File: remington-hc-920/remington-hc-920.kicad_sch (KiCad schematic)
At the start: 8 parts, among them M1 Motor_DC, SW1 SW_DPDT_x2

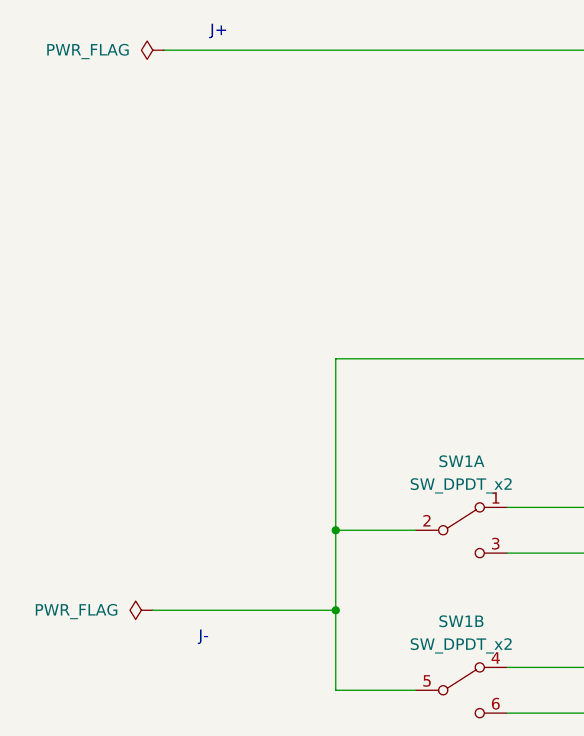
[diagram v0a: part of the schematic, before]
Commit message: Label J+/J- as charging plug input
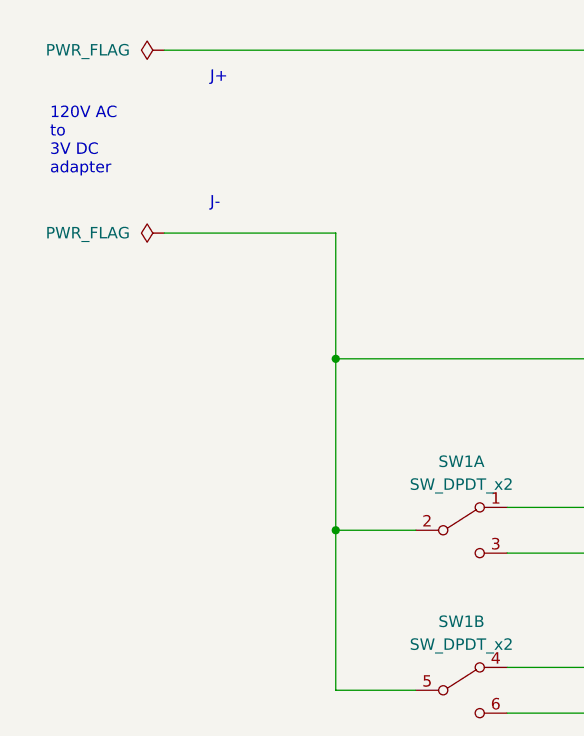
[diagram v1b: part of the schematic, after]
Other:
- note added: "120V AC to 3V DC adapter"
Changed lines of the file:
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@@
   (junction (at 199.39 115.57) (diameter 0) (color 0 0 0 0)
   )
-  (junction (at 99.06 133.35) (diameter 0) (color 0 0 0 0)
-  )
   (junction (at 162.56 121.92) (diameter 0) (color 0 0 0 0)
   )
@@
   (junction (at 99.06 124.46) (diameter 0) (color 0 0 0 0)
   )
+  (junction (at 99.06 105.41) (diameter 0) (color 0 0 0 0)
+  )
   (junction (at 138.43 105.41) (diameter 0) (color 0 0 0 0)
   )
@@
     (stroke (width 0) (type default))
   )
-  (wire (pts (xy 99.06 133.35) (xy 99.06 124.46))
-    (stroke (width 0) (type default))
-  )
   (wire (pts (xy 138.43 71.12) (xy 138.43 77.47))
     (stroke (width 0) (type default))
@@
     (stroke (width 0) (type default))
   )
-  (wire (pts (xy 99.06 124.46) (xy 99.06 105.41))
-    (stroke (width 0) (type default))
-  )
   (wire (pts (xy 138.43 87.63) (xy 138.43 90.17))
     (stroke (width 0) (type default))
@@
     (stroke (width 0) (type default))
   )
-  (wire (pts (xy 78.74 133.35) (xy 99.06 133.35))
+  (wire (pts (xy 80.01 91.44) (xy 99.06 91.44))
+    (stroke (width 0) (type default))
+  )
+  (wire (pts (xy 99.06 105.41) (xy 99.06 124.46))
     (stroke (width 0) (type default))
   )
@@
     (stroke (width 0) (type default))
   )
-  (wire (pts (xy 99.06 133.35) (xy 99.06 142.24))
+  (wire (pts (xy 99.06 124.46) (xy 99.06 142.24))
     (stroke (width 0) (type default))
   )
@@
     (stroke (width 0) (type default))
   )
+  (wire (pts (xy 99.06 91.44) (xy 99.06 105.41))
+    (stroke (width 0) (type default))
+  )
   (wire (pts (xy 99.06 142.24) (xy 107.95 142.24))
     (stroke (width 0) (type default))
@@
     (stroke (width 0) (type default))
   )
+  (text "120V AC\nto\n3V DC\nadapter" (at 67.31 85.09 0)
+    (effects (font (size 1.27 1.27)) (justify left bottom))
+  )
   (text "L+" (at 212.09 95.25 0)
     (effects (font (size 1.27 1.27)) (justify left bottom))
@@
     (effects (font (size 1.27 1.27)) (justify left bottom))
   )
-  (text "J-" (at 83.82 137.16 0)
-    (effects (font (size 1.27 1.27)) (justify left bottom))
-  )
-  (text "J+" (at 85.09 69.85 0)
+  (text "J-" (at 85.09 88.9 0)
+    (effects (font (size 1.27 1.27)) (justify left bottom))
+  )
+  (text "J+" (at 85.09 74.93 0)
     (effects (font (size 1.27 1.27)) (justify left bottom))
   )
@@
     )
   )
-  (symbol (lib_id "power:PWR_FLAG") (at 78.74 133.35 90) (unit 1)
+  (symbol (lib_id "power:PWR_FLAG") (at 80.01 91.44 90) (unit 1)
     (in_bom yes) (on_board yes) (dnp no) (fields_autoplaced)
-    (property "Reference" "#FLG02" (at 76.835 133.35 0)
-      (effects (font (size 1.27 1.27)) hide)
-    )
-    (property "Value" "PWR_FLAG" (at 74.93 133.35 90)
-      (effects (font (size 1.27 1.27)) (justify left))
-    )
-    (property "Footprint" "" (at 78.74 133.35 0)
-      (effects (font (size 1.27 1.27)) hide)
-    )
-    (property "Datasheet" "~" (at 78.74 133.35 0)
-      (effects (font (size 1.27 1.27)) hide)
-    )
+    (property "Reference" "#FLG02" (at 78.105 91.44 0)
+      (effects (font (size 1.27 1.27)) hide)
+    )
+    (property "Value" "PWR_FLAG" (at 76.2 91.44 90)
+      (effects (font (size 1.27 1.27)) (justify left))
+    )
+    (property "Footprint" "" (at 80.01 91.44 0)
+      (effects (font (size 1.27 1.27)) hide)
+    )
+    (property "Datasheet" "~" (at 80.01 91.44 0)
+      (effects (font (size 1.27 1.27)) hide)
+    )
